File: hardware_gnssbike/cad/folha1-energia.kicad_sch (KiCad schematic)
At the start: 79 parts, among them J101 HRO TYPE-C-31-M-12, J102 JST SM06B-GHS-TB, J103 JST S4B-ZR-SM4A-TF, U101 nPM1300-QEAA, U102 MAX17262REWL, U103 ADP5091ACPZ-2, U104 TPS7A0218PDQN, U105 TLV7031DCKR

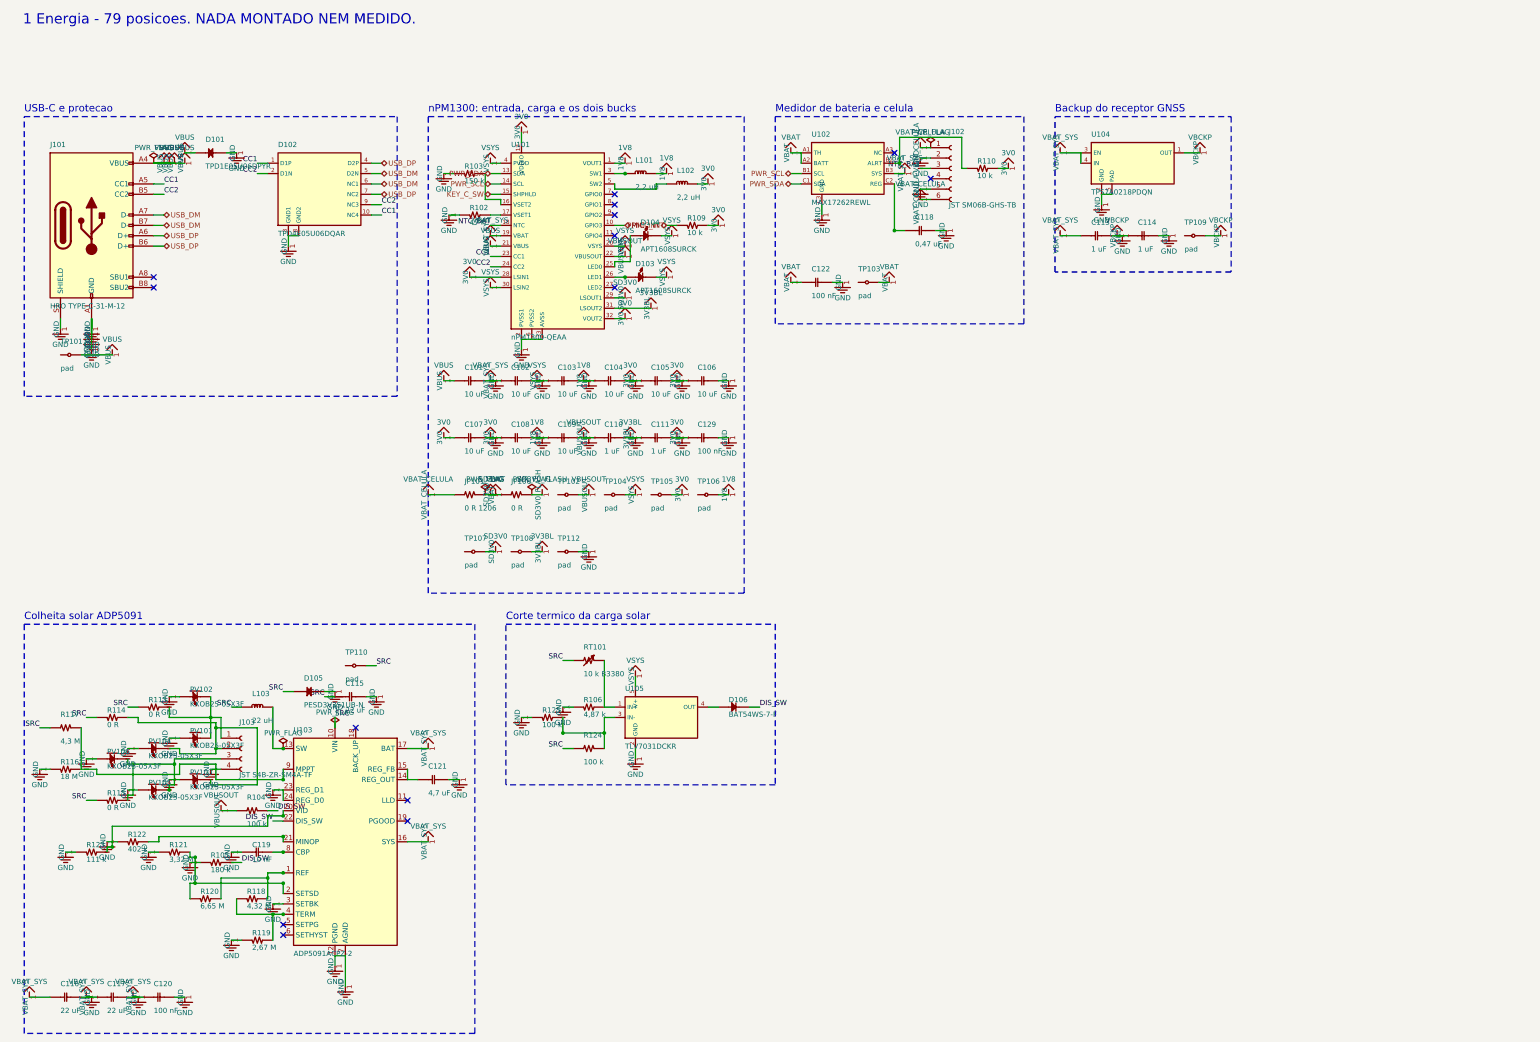
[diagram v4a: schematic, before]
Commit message: feat(hardware): spread the schematic so references, values and labels stay apart
The owner asked for the block-drawn schematic to be readable: designators
and labels were printing over each other. Power symbols now hide the pin
number and name (each printed a "1" and the rail's name twice) and point
away from their pin, lying along the line of a side pin with the name on
that line; the decoupling shelf is a row of stood-up capacitors per rail
with one wire along the tops and one symbol per row, test points standing
too; references and values sit to the right of a standing part and between
the neighbouring lines of a lying one, and block titles, part texts and
symbol names are obstacles for the router and for symbol and label
placement. Pull-ups and pull-downs of a labelled line stand past the label,
and off the corridor when the line goes on to another anchor; the labels'
room is reserved before the members are placed; the FPC connector is
mirrored to face the panel and aligned with it, its board-side wire
continuing from the label point, with the two nets of a pass-through pin
allowed to share cells; the two cells in front of every pin belong to its
net; DISP_VDD is drawn as a rail; blocks are packed by height and sheet 1
fits an A3.

The library symbol now always holds the base drawing and the instance
carries the rotation and mirror. The generator used to write the library
already flipped and the (mirror ...) token as well, applying the transform
twice, and the earlier "measurement" of (mirror x) was inverted by that.
Measured again on minimal files: (mirror y) swaps left for right, an
instance at 90 sends the left pin to the bottom, and KiCad transforms the
field justification along with the instance.

check_sch.py passes: the netlist equals nets.py pin by pin, no new ERC
error, no wire over a component. Eight nets are closed by labels where the
maze found no path inside the block, and the solar harvester and the left
of the gauge remain crowded; SCH_DEBUG=1 exp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
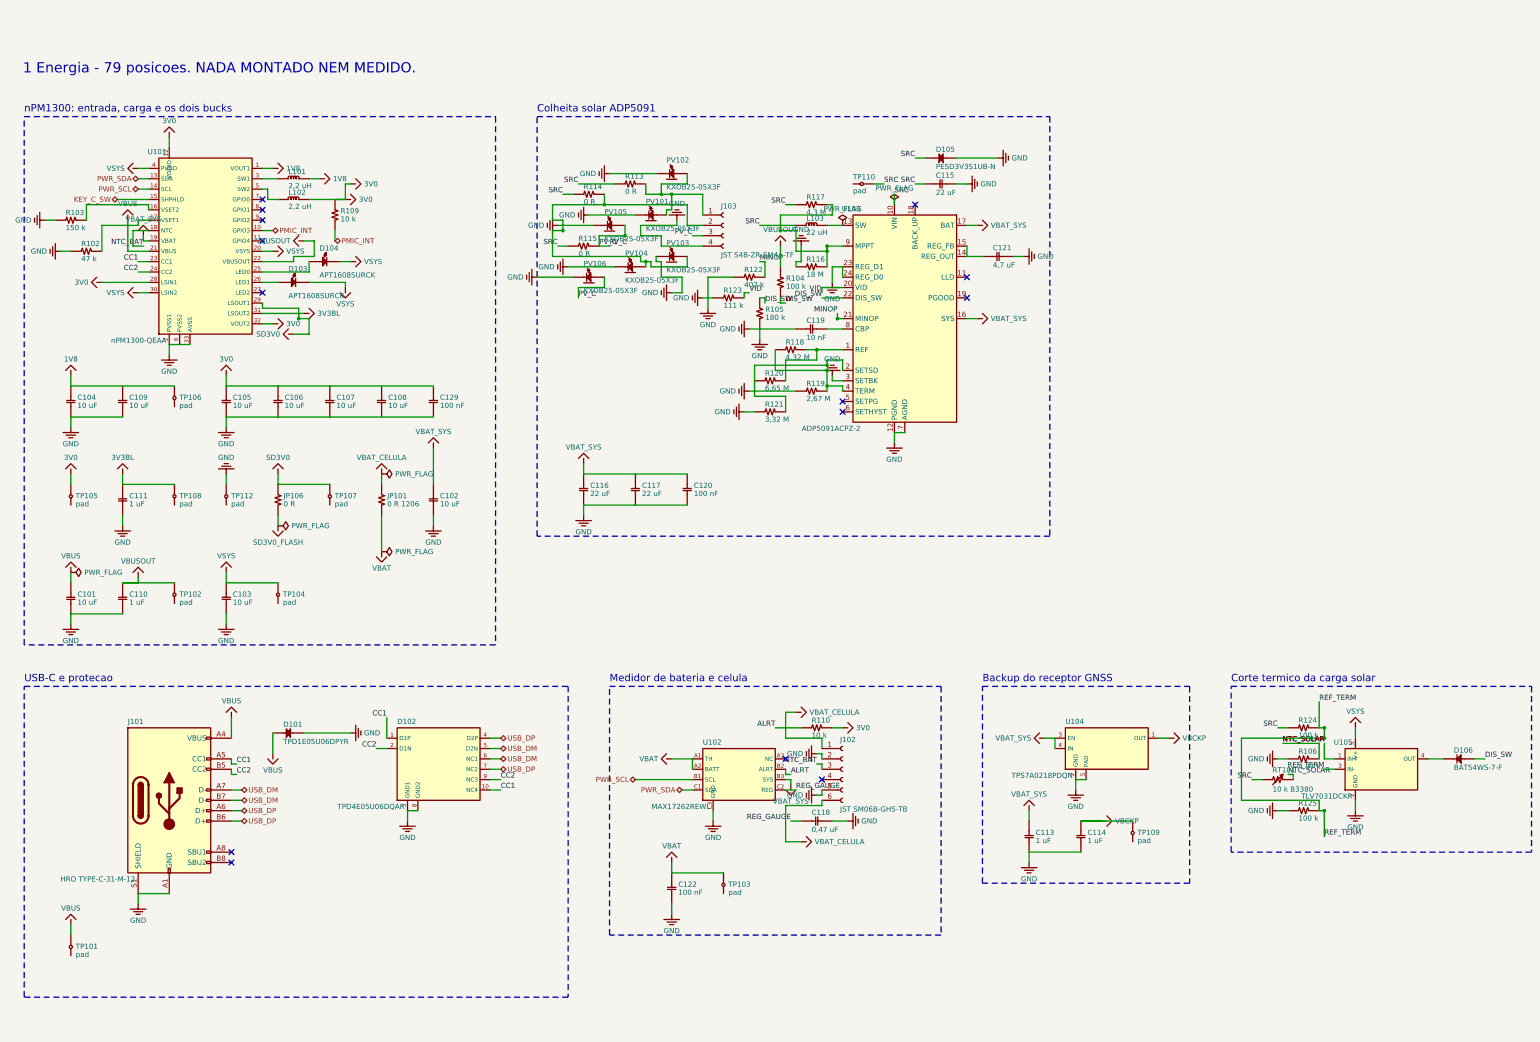
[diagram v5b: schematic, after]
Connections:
- net 1V8: no longer C101.2, C102.1, C102.2, C103.1, C103.2, C104.2, C105.1, C105.2, C106.1, C106.2, C107.1, C107.2, C108.1, C108.2, C109.2, C110.1, C110.2, C111.1, C111.2, C113.1, C113.2, C114.1, C114.2, C115.2, C116.1, C116.2, C117.1, C117.2, C118.2, C119.2, C120.1, C120.2, C121.2, C122.2, C129.1, C129.2, D101.2 (GND), D102.3 (GND1), D102.8 (GND2), D103.2 (A), D104.2 (A), D105.2 (GND), J101.A1 (GND), J101.A12 (GND), J101.B1 (GND), J101.B12 (GND), J101.S1 (SHIELD), J102.2 (Pin_2), J102.5 (Pin_5), J103.4 (Pin_4), L102.2, PV101.2 (N), PV102.2 (N), PV103.2 (N), PV104.2 (N), PV105.2 (N), PV106.2 (N), R102.2, R103.2, R104.1, R105.2, R106.2, R109.1, R110.1, R116.2, R119.2, R121.2, R122.2, R123.2, R125.2, TP102.1, TP104.1, TP105.1, TP108.1, TP109.1, TP112.1, U101.12 (VDDIO), U101.19 (VBAT), U101.2 (PVSS1), U101.20 (VSYS), U101.22 (VBUSOUT), U101.28 (LSIN1), U101.30 (LSIN2), U101.31 (LSOUT2), U101.32 (VOUT2), U101.33 (AVSS), U101.4 (PVDD), U101.6 (PVSS2), U102.B3 (SYS), U102.C3 (GND), U103.12 (PGND), U103.16 (SYS), U103.17 (BAT), U103.23 (REG_D1), U103.24 (REG_D0), U103.25 (AGND), U103.3 (SETBK), U103.7 (AGND), U104.1 (OUT), U104.2 (GND), U104.3 (EN), U104.4 (IN), U104.5 (PAD), U105.2 (GND), U105.5 (V+)
- net SD3V0: no longer C122.1, JP101.2, TP103.1, U102.A1 (TH), U102.A2 (BATT)
- net PV_C: now reaches J103.3 (Pin_3), PV105.1 (P), PV106.1 (P), R115.1
- net NTC_SOLAR: now reaches R106.1, RT101.2, U105.1 (IN+)
- net REF_TERM: now reaches R124.2, R125.1, U105.3 (IN-)
- net VID: now reaches R123.1, U103.20 (VID)
- net REG_GAUGE: now reaches C118.1, U102.C2 (REG)
- net ALRT: now reaches R110.2, U102.B2 (ALRT)
- net MINOP: now reaches R122.1, U103.21 (MINOP)
- new net 3V0: C105.1, C106.1, C107.1, C108.1, C129.1, L102.2, R109.1, R110.1, TP105.1, U101.12 (VDDIO), U101.28 (LSIN1), U101.32 (VOUT2)
- new net 3V3BL: C111.1, TP108.1, U101.31 (LSOUT2)
- new net GND: C101.2, C102.2, C103.2, C104.2, C105.2, C106.2, C107.2, C108.2, C109.2, C110.2, C111.2, C113.2, C114.2, C115.2, C116.2, C117.2, C118.2, C119.2, C120.2, C121.2, C122.2, C129.2, D101.2 (GND), D102.3 (GND1), D102.8 (GND2), D105.2 (GND), J101.A1 (GND), J101.A12 (GND), J101.B1 (GND), J101.B12 (GND), J101.S1 (SHIELD), J102.2 (Pin_2), J102.5 (Pin_5), J103.4 (Pin_4), PV101.2 (N), PV102.2 (N), PV103.2 (N), PV104.2 (N), PV105.2 (N), PV106.2 (N), R102.2, R103.2, R105.2, R106.2, R116.2, R119.2, R121.2, R122.2, R123.2, R125.2, TP112.1, U101.2 (PVSS1), U101.33 (AVSS), U101.6 (PVSS2), U102.C3 (GND), U103.12 (PGND), U103.23 (REG_D1), U103.24 (REG_D0), U103.25 (AGND), U103.3 (SETBK), U103.7 (AGND), U104.2 (GND), U104.5 (PAD), U105.2 (GND)
- new net VBAT: C122.1, JP101.2, TP103.1, U102.A1 (TH), U102.A2 (BATT)
- new net VBAT_SYS: C102.1, C113.1, C116.1, C117.1, C120.1, U101.19 (VBAT), U102.B3 (SYS), U103.16 (SYS), U103.17 (BAT), U104.3 (EN), U104.4 (IN)
- new net VBCKP: C114.1, TP109.1, U104.1 (OUT)
- new net VBUSOUT: C110.1, R104.1, TP102.1, U101.22 (VBUSOUT)
- new net VSYS: C103.1, D103.2 (A), D104.2 (A), TP104.1, U101.20 (VSYS), U101.30 (LSIN2), U101.4 (PVDD), U105.5 (V+)
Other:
- moved on the sheet: C101, C102, C103, C104, C105, C106, C107, C108, C109, C110, C111, C113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

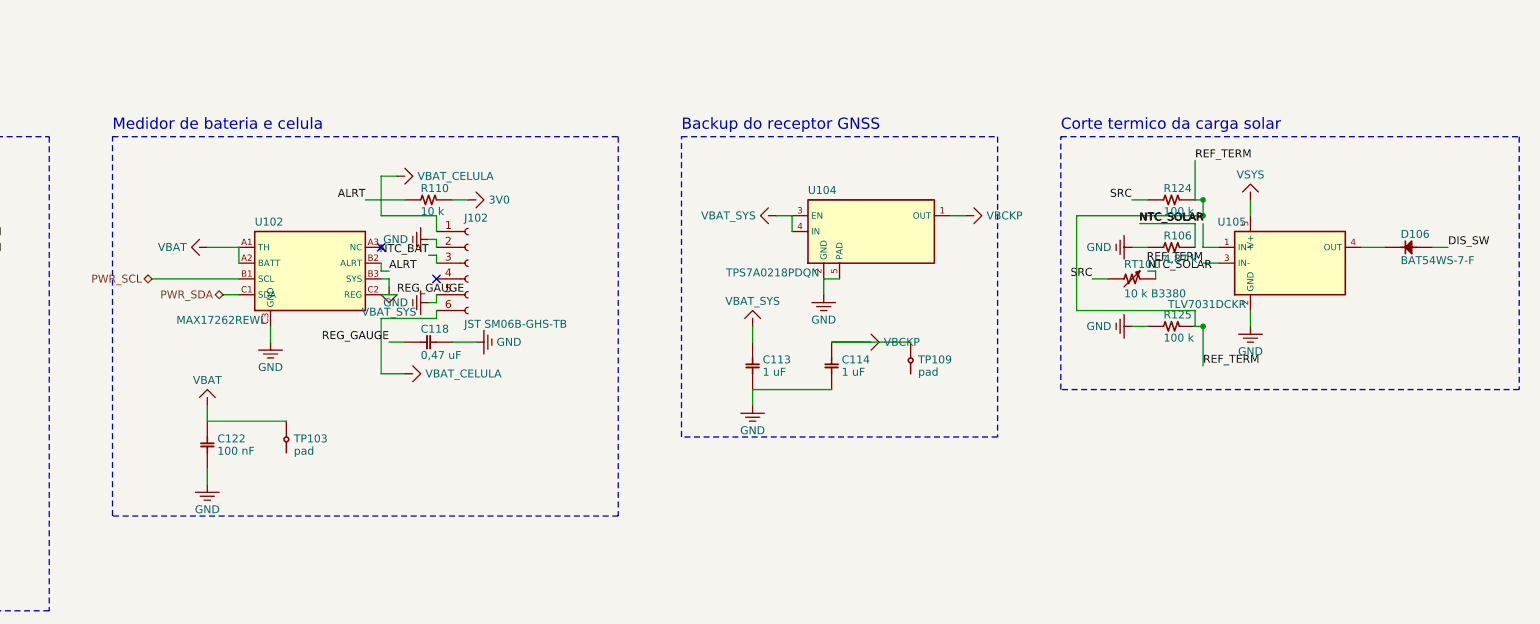
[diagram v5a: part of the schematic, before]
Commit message: fix(hardware): regenerate the schematic for the SH battery connector
parts.py has given J102 as the JST SH SM06B-SRSS-TB since the afternoon
of 2026-09-26, but the sheets and the PDF still drew the GH part because
check_sch.py did not run after the change. Regenerated through the chain:
check_sch.py passes and the PDF shows the SH connector.
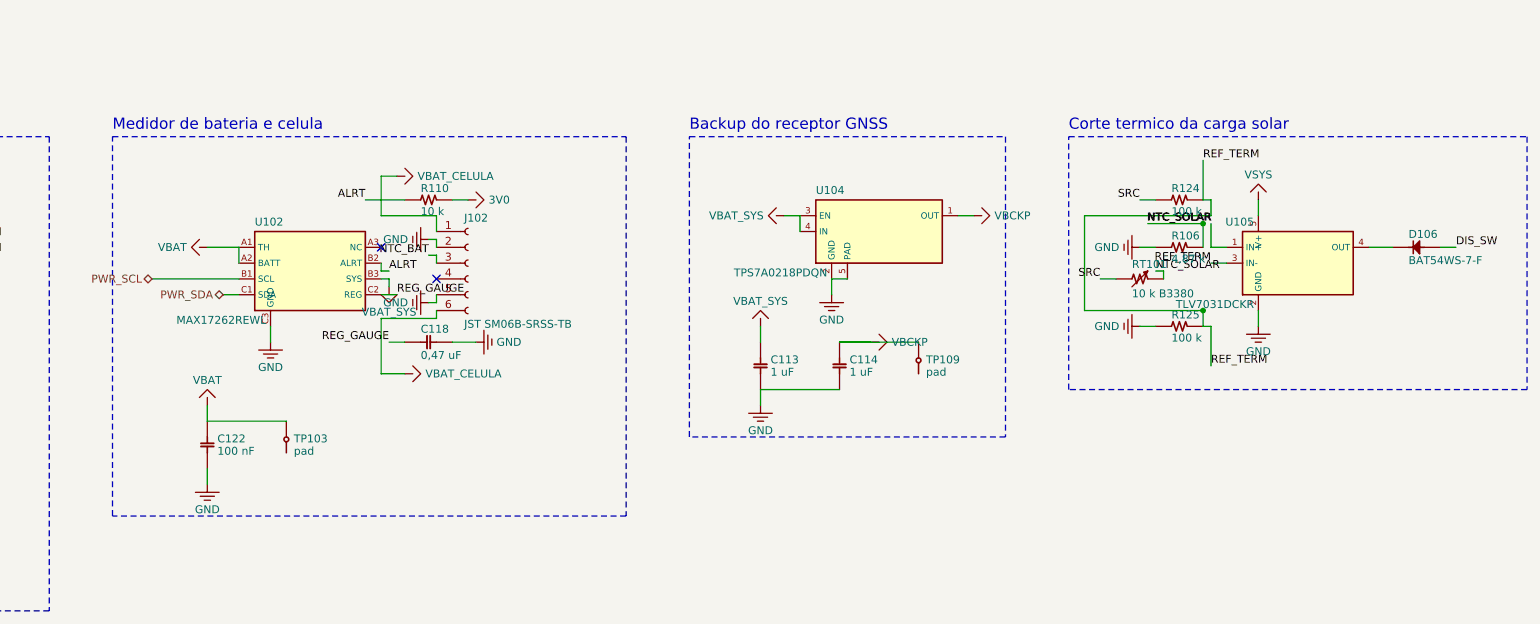
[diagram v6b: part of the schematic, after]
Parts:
- J102: value JST SM06B-GHS-TB -> JST SM06B-SRSS-TB; footprint Connector_JST:JST_GH_SM06B-GHS-TB_1x06-1MP_P1.25mm_Horizontal -> Connector_JST:JST_SH_SM06B-SRSS-TB_1x06-1MP_P1.00mm_Horizontal
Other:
- moved on the sheet: C113, C114, D106, R106, R124, R125, RT101, TP109, U104, U105

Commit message: feat(hardware): apply the schematic review, take either display, review the case
Apply the corrections the owner approved on 2026-10-18, in the
generators: the BMP585 land from figure 29, the RGB LED land unmirrored,
the TLV7031DCKR renumbered and fed from VBAT_SYS, the common pad of
JP301 in the middle, the OPT3001 exposed pad, the Murata land for the
buck inductors, 10 uF on PVDD and 3V3BL, a 24 V TVS on VBUS, the flash
on 3V0, pin-1 marks, the charge LEDs in the key row, the TVS next to
their connectors, the USB-C on the maker's edge line, the Same Sky
buzzer in place of the last-time-buy Murata, and an LCSC code on every
fitted part.

The board takes the JDI or the Sharp on one dual-contact Molex 503480:
JP401 picks 3V0 or 5V0, and a TPS610997 boost feeds the Sharp. A second
blind check found the connector drawn backwards (the tail enters on the
nail side); the land, the circuit order and the boost placement follow
the drawings now.

The router finds its way further: unique UUIDs per footprint, so the
DRC names the right pads; the chip antenna's own nets inside its
keep-out; JP301 turned so the two RF lines do not cross; ground vias
outside the dense chips, bent and geometrically checked ground stubs,
and a pass with the power rails first. The DRC reports no error; 60
items are still unconnected.

The case is reviewed part by part (hardware_gnssbike/12): the solar
module pockets follow the datasheet's +-0.3 mm (the case grows to 64 mm),
the keys stop 0.15 mm under the membrane, and the light sensor gets a
sealed window. The sealing of the USB-C, the floor holes and the lid
seam is left to the owner. The documents follow parts.py.

Nothing is fabricated, and the routing is still open.
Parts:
- D101: value TPD1E05U06DPYR -> PESD24VS1UL,315; footprint gnssbike:ESD761_X1SON-2_1x0.6mm -> Diode_SMD:D_SOD-882
- L101, L102: footprint Inductor_SMD:L_0805_2012Metric -> Inductor_SMD:L_Murata_DFE201610P
- R123: value 111 k -> 110 k
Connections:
- net 3V0: now also JP106.1; no longer C107.1, C108.1
- net 3V3BL: now also C108.1
- net NTC_SOLAR: now also U105.3 (IN+); no longer U105.1 (IN+)
- net REF_TERM: now also U105.4 (IN-); no longer U105.3 (IN-)
- net SD3V0: no longer JP106.1
- net VBAT_SYS: now also U105.5 (V+)
- net VSYS: now also C107.1; no longer U105.5 (V+)
- net at D106.2 (A): now also U105.1 (OUT); no longer U105.4 (OUT)
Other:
- note added: "Outros"
- moved on the sheet: C101, C102, C103, C107, C108, C110, C111, C113, C114, C118, C122, C129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

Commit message: fix(hardware): change the schematic where the board could not route
Three changes the routing of 2026-10-19 asked for, each checked against
the part's datasheet:

- ALRT of the MAX17262 goes to GND, as the datasheet asks when the alert
  is not used, and its 10 k pull-up R110 is gone: no pin read it, and the
  middle bump of a 0.4 mm WLP could only reach it through a via in pad.
- The USB pair crosses the TPD4E05U06 by the channels in the order it
  arrives (D+ on pins 5 and 6, D- on 4 and 7). The four channels are the
  same diode to ground; with the pin names followed, the pair could only
  reach the module by crossing itself on a layer where it takes no via.
- The chip antenna's tuning capacitors sit where Unictron's figures 5-1
  and 8-1 put them, lying on the board edge at the two ends of the
  cut-out, with C305 (pin 1, wide side) at 6.8 pF and C306 at 2.7 pF.
  They stood in the middle of the cut-out with the values swapped, and
  the ground pad of C305 had no ground within reach.

check_sch.py regenerates the sheets and passes, with the open-drain ALRT
on the ground node accepted by the ERC; the schematic PDF is exported
again. Bench tuning of the antenna is still to be done.
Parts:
- removed R110: 10 k, Resistor_SMD:R_0402_1005Metric, symbol gnssbike:R110
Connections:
- net ALRT is gone; now on net GND: U102.B2 (ALRT)
- net USB_DM: now also D102.4 (D2P), D102.7 (NC2); no longer D102.5 (D2N), D102.6 (NC1)
- net USB_DP: now also D102.5 (D2N), D102.6 (NC1); no longer D102.4 (D2P), D102.7 (NC2)
- net REG_GAUGE: no longer names the net of C118.1, U102.C2 (REG)
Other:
- note added: "1 Energia - 78 posicoes. NADA MONTADO NEM MEDIDO."
- note removed: "1 Energia - 79 posicoes. NADA MONTADO NEM MEDIDO."
- moved on the sheet: C118, C122, J102, TP103, U102
